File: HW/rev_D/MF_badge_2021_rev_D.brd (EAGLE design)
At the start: 61 x 100.5 mm, 166 parts, among them IC1 MCP73831, J1 HRO_31_M_12_USB_C, Q1 SI1308EDL-T1-GE3, Q2 DMG3415U-7, Q3 DMG3415U-7, Q4 DMG3415U-7, Q5 Si2305, U1 ESP32-S2-WROOM, U2 AP2112K-3.3, X1 CAPTOUCH_10MM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

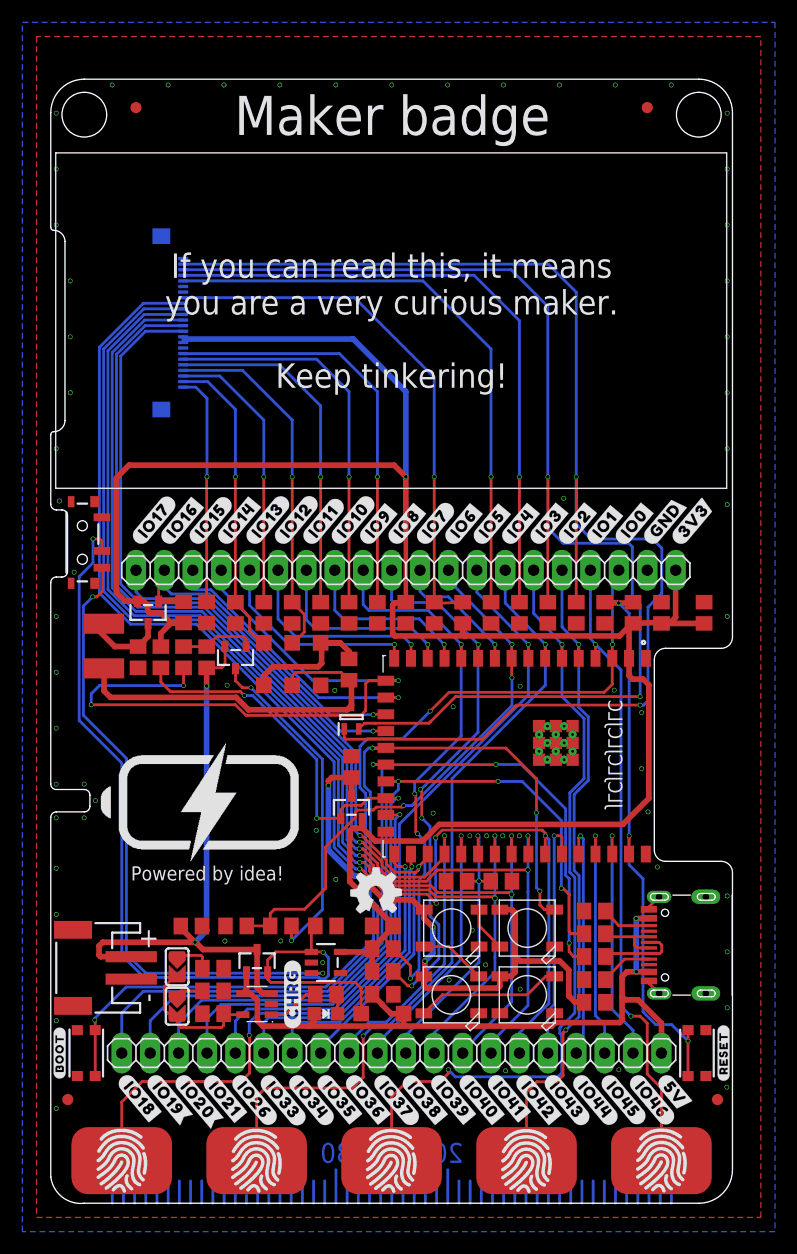
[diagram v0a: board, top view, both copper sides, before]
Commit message: Error fix for 3V3 line at e-ink display
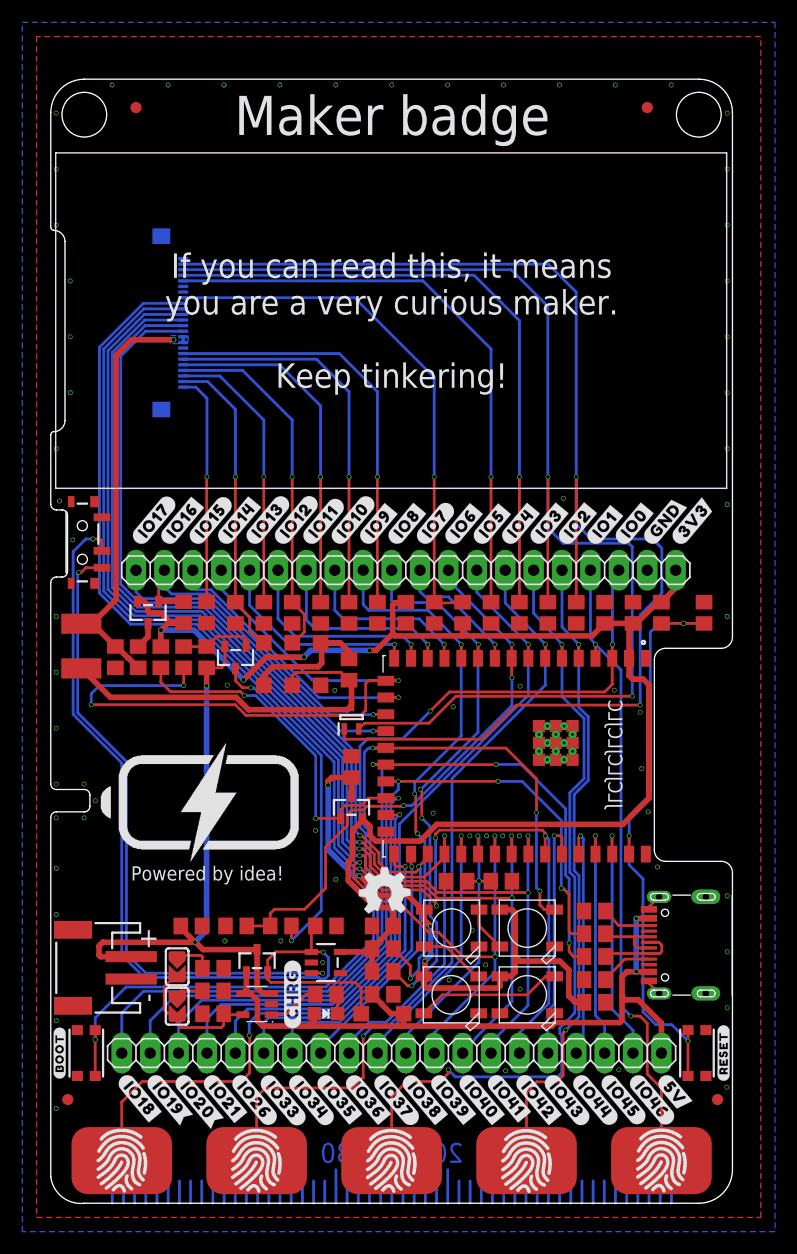
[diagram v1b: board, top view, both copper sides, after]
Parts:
- added R19: 10R, rcl:R0805
- moved C17 8.89 mm to (58.4, 52.8), turned to 90 degrees
- moved C19 6.35 mm to (52.1, 52.8)
- moved C18 5.08 mm to (49.5, 52.8)
- moved R8 2.54 mm to (54.6, 52.8), turned to 90 degrees
- moved C12 2.03 mm to (5.78, 48.8)
- moved L1 2.03 mm to (2.73, 49.8)
- moved GOLD_ORB_SM1 0.76 mm to (29.8, 27.7)
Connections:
- new net N$27: C12.1, L1.1, R19.1, U$1.15, U$1.16
- net +3V3: no longer U$1.15, U$1.16
- net N$26: now also R19.2; no longer C12.1, L1.1
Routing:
- net +3V3: track 192.5 -> 131.7 mm, vias 1 -> 4
- net N$27: track 0.00 -> 38.8 mm, vias 0 -> 1
- net N$26: track 7.40 -> 2.42 mm
- net IO39_RST: track 104.6 -> 108.3 mm
- net EN: track 50.9 -> 53.2 mm
- net N$18: track 56.4 -> 57.5 mm
- net N$10: track 113.3 -> 112.3 mm
- net N$19: track 33.7 -> 34.5 mm
- net N$9: track 83.2 -> 84.0 mm
- net IO0: track 86.1 -> 86.9 mm
- net IO42_BUSY: track 115.9 -> 116.5 mm
- added copper zone on layer 16, net N$27

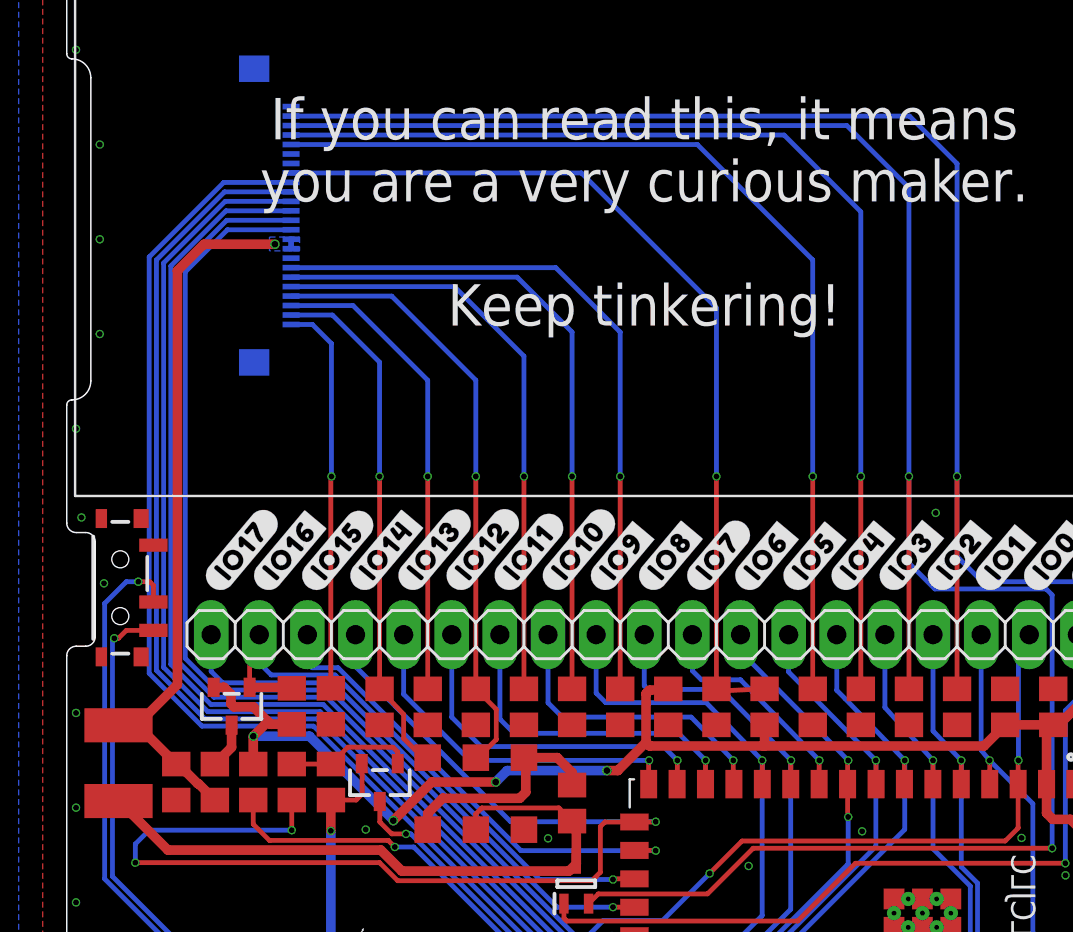
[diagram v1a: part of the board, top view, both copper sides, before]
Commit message: Moved 3V3 for e-ink power pins before R19
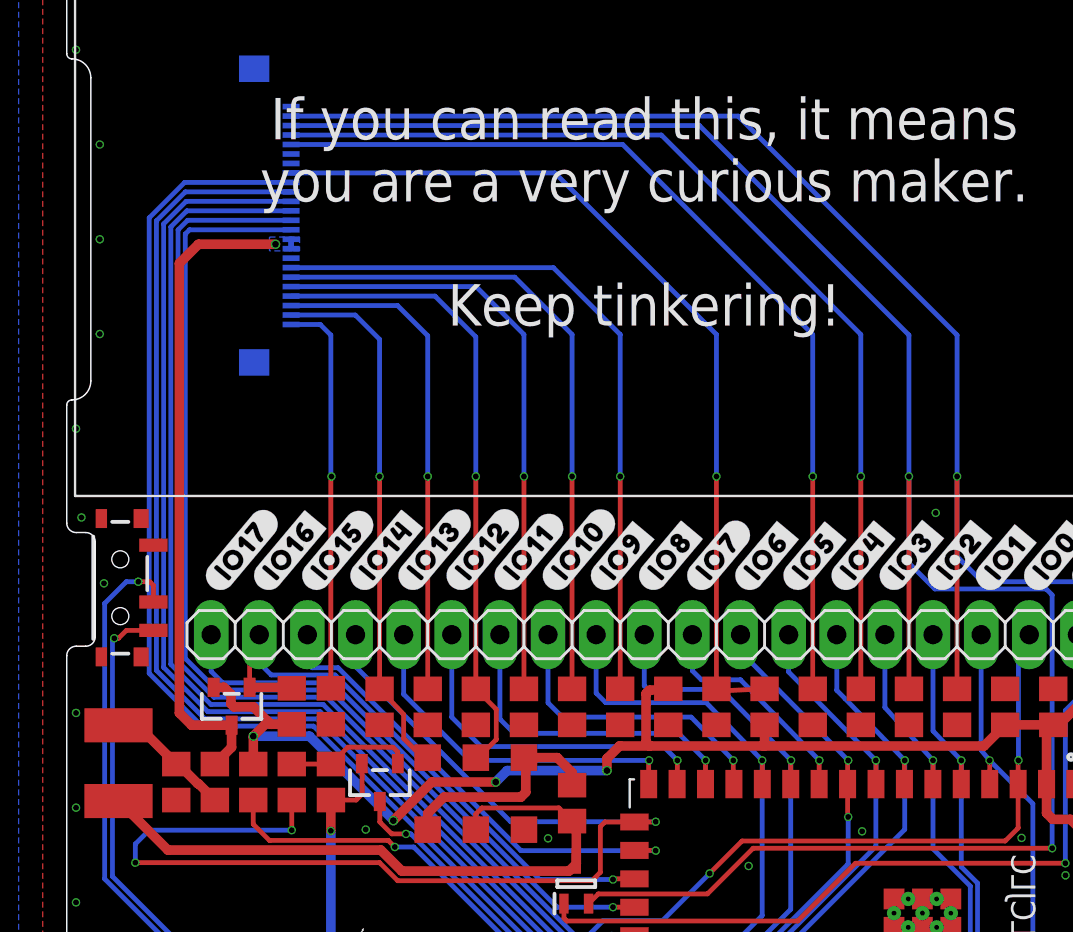
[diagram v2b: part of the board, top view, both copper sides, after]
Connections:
- removed net N$26: Q4.3, R19.2
- new net N$78: C12.1, L1.1, R19.1
- net N$27: now also Q4.3, R19.2; no longer C12.1, L1.1, R19.1
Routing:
- net N$78: track 0.00 -> 6.72 mm
- net N$13: track 120.1 -> 114.8 mm
- net N$10: track 112.3 -> 107.7 mm
- net N$12: track 56.9 -> 53.1 mm
- net N$27: track 38.8 -> 35.2 mm
- net N$26: track 2.42 -> 0.00 mm
- net N$11: track 52.7 -> 50.4 mm
- net N$3: track 25.1 -> 26.5 mm
- net N$4: track 32.5 -> 33.8 mm
- net IO42_BUSY: track 116.5 -> 117.7 mm
- net IO41_CS: track 104.4 -> 105.6 mm
- net IO39_RST: track 108.3 -> 109.5 mm
- net IO36_SCK: track 99.2 -> 100.4 mm
- net IO40_DC: track 104.8 -> 106.0 mm
- net IO35_MOSI: track 91.1 -> 92.3 mm
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
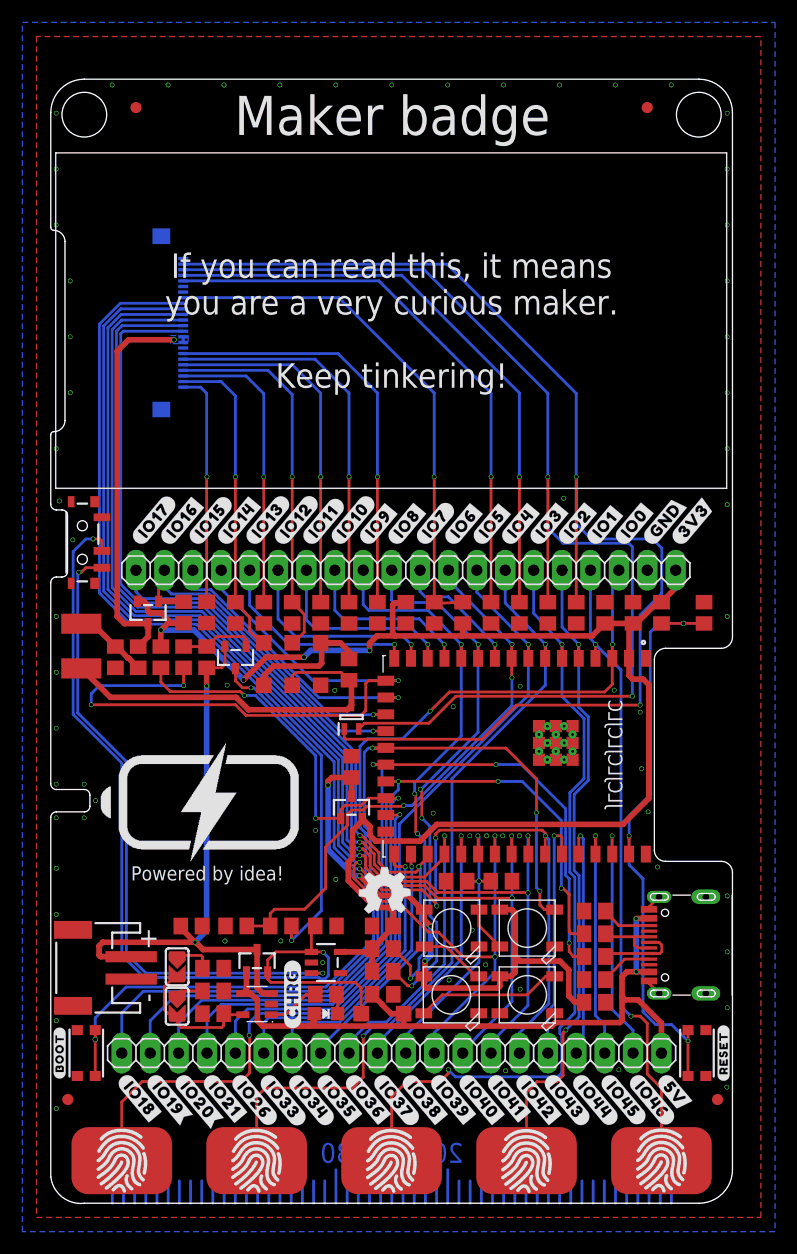
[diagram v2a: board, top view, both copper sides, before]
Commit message: Update
- added schematics for all versions
- added protoshield files
- added files for rev. D
- README update
- removed unnecessary files
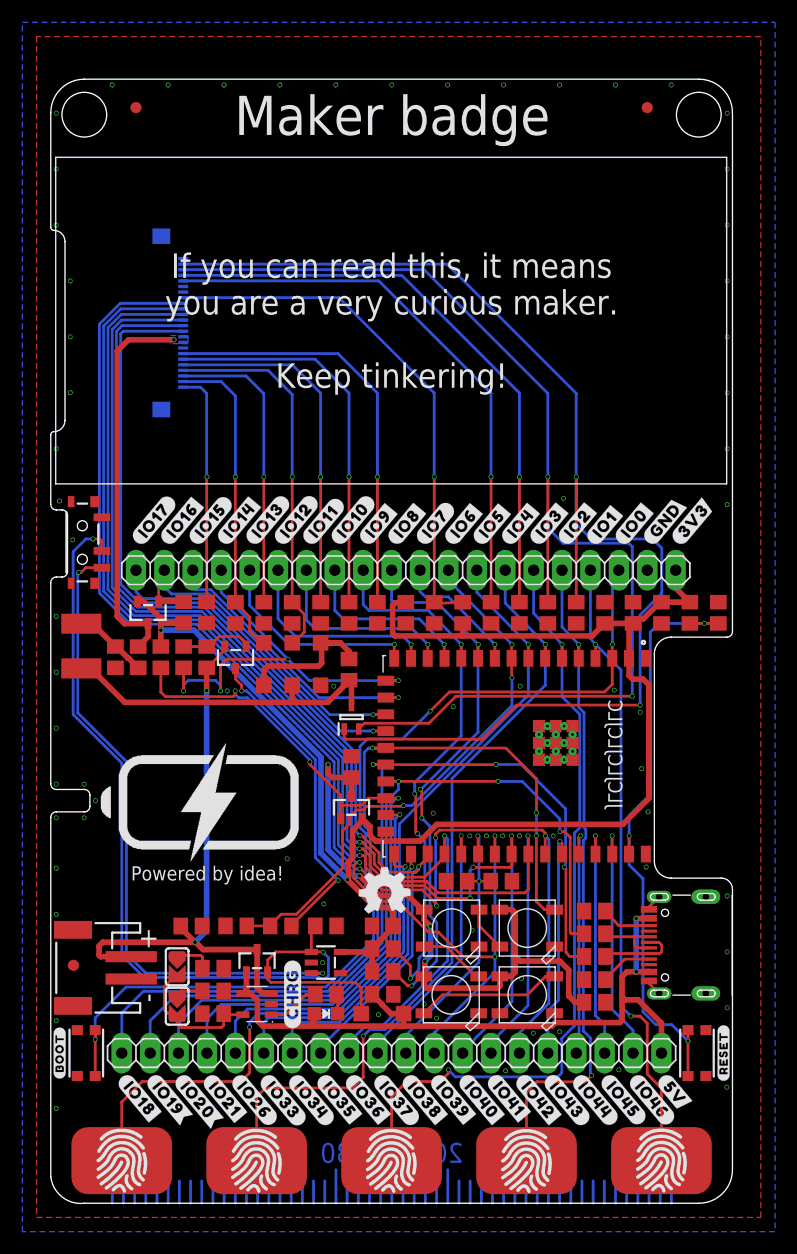
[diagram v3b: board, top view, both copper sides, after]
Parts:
- removed FID4: FIDUCIAL_1MM, microbuilder:FIDUCIAL_1MM
- added C23: 10uF, rcl:C0805
- C14, C20: value 10uF -> 22uF
- C18: value 10uF -> 47uF
- FID1, FID2, FID3: value FIDUCIAL_1MM -> FIDUCIAL""
- moved FID3 12.0 mm to (2.02, 21.3)
- moved R8 2.54 mm to (57.1, 52.8)
- moved C17 1.27 mm to (59.7, 52.8)
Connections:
- net +3V3: now also C23.1
- net GND: now also C23.2
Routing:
- net IO14: track 62.6 -> 37.5 mm, vias 3 -> 4
- net +3V3: track 132.2 -> 140.5 mm, vias 4 -> 2
- net N$19: track 34.5 -> 29.9 mm
- net IO40_DC: track 106.0 -> 109.7 mm, vias 3 -> 4
- net IO41_CS: track 105.6 -> 108.9 mm, vias 3 -> 2
- net V+: track 53.5 -> 55.8 mm
- net N$79: track 30.5 -> 28.9 mm
- net IO2: track 58.7 -> 60.2 mm
- net IO21: track 67.9 -> 66.4 mm
- net IO43: track 21.9 -> 20.6 mm
- net IO6: track 49.7 -> 48.7 mm
- net IO3: track 71.9 -> 71.0 mm
- net BAT+: track 53.7 -> 52.9 mm
- net EN: track 53.2 -> 53.8 mm
- net N$27: track 35.2 -> 34.7 mm
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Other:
- outline, holes or cut-outs redrawn
